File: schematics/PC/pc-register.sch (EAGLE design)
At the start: 26 parts

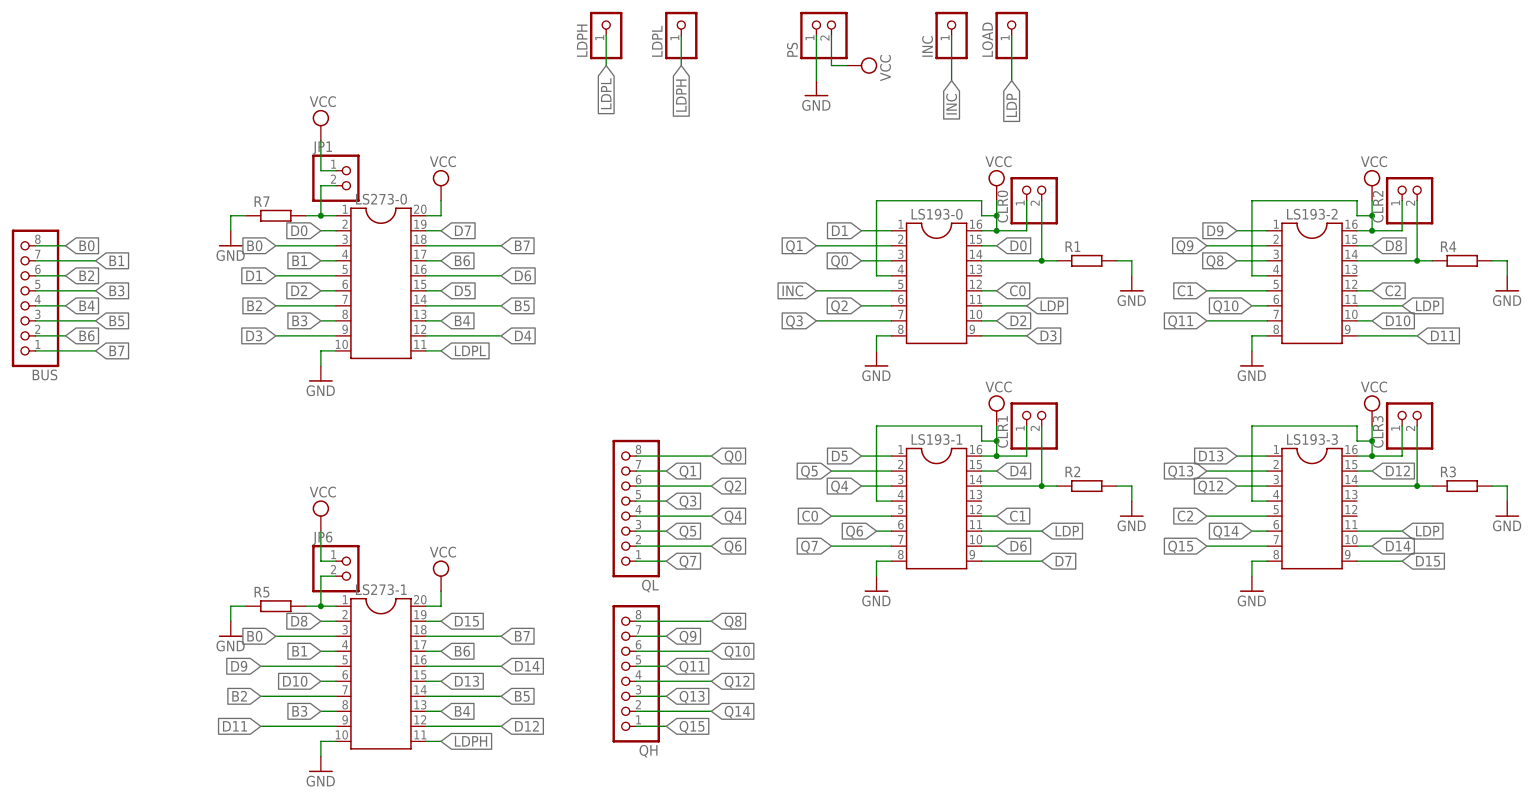
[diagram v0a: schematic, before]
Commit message: Schematic for PC, PC-register and PC-bus.
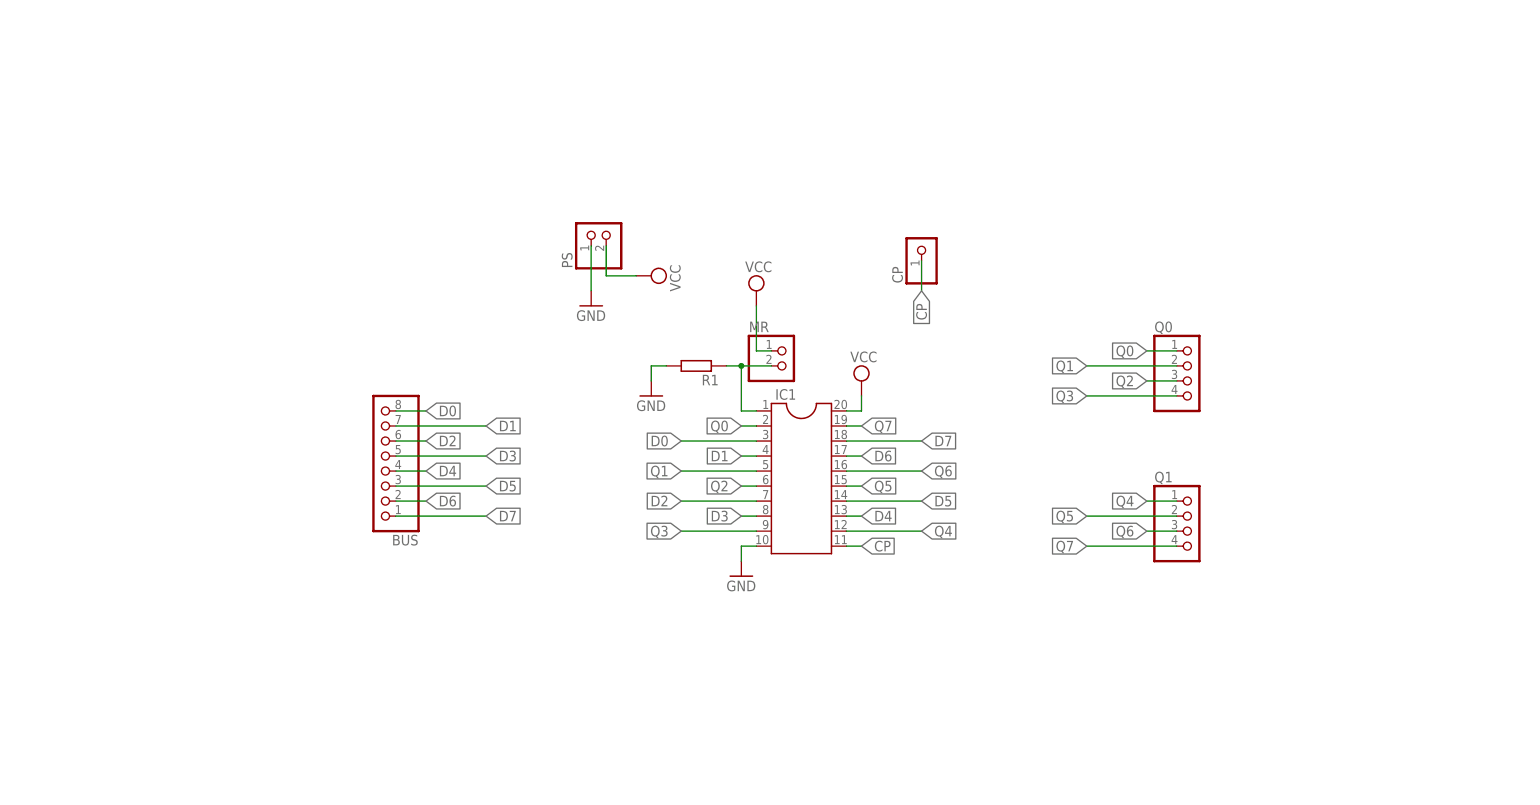
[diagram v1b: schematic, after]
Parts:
- removed CLR0, CLR1, CLR2, CLR3, JP1, JP6: (no value), pinhead:PINHD-1X2
- removed INC, LDPH, LDPL, LOAD: (no value), pinhead:PINHD-1X1
- removed LS193-0, LS193-1, LS193-2, LS193-3: (no value), ic-package:DIL16S
- removed LS273-0, LS273-1: (no value), ic-package:DIL20S
- removed QH, QL: (no value), pinhead:PINHD-1X8
- removed R2, R3, R4, R5, R7: (no value), rcl:R-EU_0204/7
- added CP: (no value), pinhead:PINHD-1X1
- added IC1: (no value), ic-package:DIL20S
- added MR: (no value), pinhead:PINHD-1X2
- added Q0, Q1: (no value), pinhead:PINHD-1X4
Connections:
- removed net B0: BUS.8, LS273-0.3, LS273-1.3
- removed net B1: BUS.7, LS273-0.4, LS273-1.4
- removed net B2: BUS.6, LS273-0.7, LS273-1.7
- removed net B3: BUS.5, LS273-0.8, LS273-1.8
- removed net B4: BUS.4, LS273-0.13, LS273-1.13
- removed net B5: BUS.3, LS273-0.14, LS273-1.14
- removed net B6: BUS.2, LS273-0.17, LS273-1.17
- removed net B7: BUS.1, LS273-0.18, LS273-1.18
- removed net C0: LS193-0.12, LS193-1.5
- removed net C1: LS193-1.12, LS193-2.5
- removed net C2: LS193-2.12, LS193-3.5
- removed net D10: LS193-2.10, LS273-1.6
- removed net D11: LS193-2.9, LS273-1.9
- removed net D12: LS193-3.15, LS273-1.12
- removed net D13: LS193-3.1, LS273-1.15
- removed net D14: LS193-3.10, LS273-1.16
- removed net D15: LS193-3.9, LS273-1.19
- removed net D8: LS193-2.15, LS273-1.2
- removed net D9: LS193-2.1, LS273-1.5
- removed net INC: INC.1, LS193-0.5
- removed net LDP: LOAD.1, LS193-0.11, LS193-1.11, LS193-2.11, LS193-3.11
- removed net LDPH: LDPL.1, LS273-1.11
- removed net LDPL: LDPH.1, LS273-0.11
- removed net N$1: CLR0.2, LS193-0.14, R1.1
- removed net N$2: JP1.2, LS273-0.1, R7.2
- removed net N$3: CLR2.2, LS193-2.14, R4.1
- removed net N$5: CLR3.2, LS193-3.14, R3.1
- removed net N$8: CLR1.2, LS193-1.14, R2.1
- removed net N$9: JP6.2, LS273-1.1, R5.2
- removed net Q10: LS193-2.6, QH.6
- removed net Q11: LS193-2.7, QH.5
- removed net Q12: LS193-3.3, QH.4
- removed net Q13: LS193-3.2, QH.3
- removed net Q14: LS193-3.6, QH.2
- removed net Q15: LS193-3.7, QH.1
- removed net Q8: LS193-2.3, QH.8
- removed net Q9: LS193-2.2, QH.7
- new net CLR: IC1.1, MR.2, R1.1
- new net CP: CP.1, IC1.11
- net D0: now also BUS.8, IC1.3; no longer LS193-0.15, LS273-0.2
- net D1: now also BUS.7, IC1.4; no longer LS193-0.1, LS273-0.5
- net D2: now also BUS.6, IC1.7; no longer LS193-0.10, LS273-0.6
- net D3: now also BUS.5, IC1.8; no longer LS193-0.9, LS273-0.9
- net D4: now also BUS.4, IC1.13; no longer LS193-1.15, LS273-0.12
- net D5: now also BUS.3, IC1.14; no longer LS193-1.1, LS273-0.15
- net D6: now also BUS.2, IC1.17; no longer LS193-1.10, LS273-0.16
- net D7: now also BUS.1, IC1.18; no longer LS193-1.9, LS273-0.19
- net GND: now also IC1.10; no longer LS193-0.8, LS193-1.8, LS193-2.8, LS193-3.8, LS273-0.10, LS273-1.10, R2.2, R3.2, R4.2, R5.1, R7.1
- net Q0: now also IC1.2, Q0.1; no longer LS193-0.3, QL.8
- net Q1: now also IC1.5, Q0.2; no longer LS193-0.2, QL.7
- net Q2: now also IC1.6, Q0.3; no longer LS193-0.6, QL.6
- net Q3: now also IC1.9, Q0.4; no longer LS193-0.7, QL.5
- net Q4: now also IC1.12, Q1.1; no longer LS193-1.3, QL.4
- net Q5: now also IC1.15, Q1.2; no longer LS193-1.2, QL.3
- net Q6: now also IC1.16, Q1.3; no longer LS193-1.6, QL.2
- net Q7: now also IC1.19, Q1.4; no longer LS193-1.7, QL.1
- net VCC: now also IC1.20, MR.1; no longer CLR0.1, CLR1.1, CLR2.1, CLR3.1, JP1.1, JP6.1, LS193-0.16, LS193-0.4, LS193-1.16, LS193-1.4, LS193-2.16, LS193-2.4, LS193-3.16, LS193-3.4, LS273-0.20, LS273-1.20
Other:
- moved on the sheet: BUS, PS, R1
